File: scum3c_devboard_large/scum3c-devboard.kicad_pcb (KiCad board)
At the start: 2 copper layers, 39.3 x 76.2 mm, 62 parts, among them J1 CONSMA001-SMD-G-T, J2 47346-0001, J3 Conn_02x06_Odd_Even, J4 Conn_01x23, J5 Conn_02x02_Odd_Even, J6 Conn_02x02_Odd_Even, U1 Perfboard, U2 FT231XS-U, U3 74AVC1T45GS,132, U4 74AVC1T45GS,132, U5 LP5907MFX-1.5, U6 S-85S1AB10-I6T1U, U7 S-85S1AB15-I6T1U, U8 scum3, U9AB1 MPU-9250

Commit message: ready for merge
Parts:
- removed C12, C8: LED, Capacitor_SMD:C_0402_1005Metric
- removed C13, C14, C15, C16, C17, C18, C19, C20, C21, C22, C24: NP, Capacitor_SMD:C_0402_1005Metric
- removed NT1: Net-Tie_2, NetTie:NetTie-2_SMD_Pad0.5mm
- removed R12, R13, R14, R5, R6: NP, Resistor_SMD:R_0402_1005Metric
- added D1: LED, LED_SMD:LED_0402_1005Metric, F.Cu at (209.9, 95.6)
- added D2: LED, LED_SMD:LED_0402_1005Metric, F.Cu at (207.0, 87.0)
- added IC1: 74AVC4TD245PW,118, SamacSys_Parts:SOP65P640X110-16N, F.Cu at (223.1, 122.7)
- added IC2: 74AVC4TD245PW,118, SamacSys_Parts:SOP65P640X110-16N, F.Cu at (223.0, 96.5)
- added J7: Conn_01x03, Connector_PinHeader_2.54mm:PinHeader_1x03_P2.54mm_Vertical, F.Cu at (201.5, 112.5)
- added J8: Conn_01x03, Connector_PinHeader_2.54mm:PinHeader_1x03_P2.54mm_Vertical, F.Cu at (205.2, 116.5)
- H1, H2, H3, H4: footprint MountingHole:MountingHole_2.7mm -> MountingHole:MountingHole_2.7mm_M2.5
- J4: value Conn_01x23 -> Conn_01x22; footprint Connector_PinHeader_2.54mm:PinHeader_1x23_P2.54mm_Vertical -> Connector_PinHeader_2.54mm:PinHeader_1x22_P2.54mm_Vertical
- J5: value Conn_02x02_Odd_Even -> Conn_02x04_Odd_Even; footprint Connector_PinHeader_2.54mm:PinHeader_2x02_P2.54mm_Vertical -> Connector_PinHeader_2.54mm:PinHeader_2x04_P2.54mm_Vertical
- J6: value Conn_02x02_Odd_Even -> Conn_01x03; footprint Connector_PinHeader_2.54mm:PinHeader_2x02_P2.54mm_Vertical -> Connector_PinHeader_2.54mm:PinHeader_1x03_P2.54mm_Vertical
- moved J5 51.3 mm to (196.5, 119.9)
- moved J6 51.2 mm to (201.5, 116.2)
- moved C25 48.0 mm to (220.2, 127.0)
- moved L2 48.0 mm to (221.8, 127.5)
- moved U6 48.0 mm to (224.4, 127.0)
- moved C9 48.0 mm to (226.4, 127.1), turned to 270 degrees
- moved U1 37.4 mm to (201.5, 75.4), turned to 90 degrees
- moved C23 24.8 mm to (201.7, 124.5), turned to 90 degrees
- moved U7 20.1 mm to (203.7, 125.3), turned to 180 degrees
- moved L3 15.0 mm to (206.3, 124.7), turned to 180 degrees
- moved C26 14.2 mm to (220.2, 88.2)
- moved C29 14.2 mm to (223.2, 87.9)
- moved U9AB1 14.2 mm to (224.0, 90.7)
- moved C27 14.1 mm to (225.9, 88.0)
- moved U3 12.8 mm to (217.6, 92.5), turned to 0 degrees
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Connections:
- C28 pad 1: +VBAT -> /VBAT_TEENSY
- C3 pad 1: +VBAT -> /VBAT_USB
- J4 pad 1: GND -> +VIN
- J4 pad 10: /3WB_CLK -> /3WB_ENB
- J4 pad 11: /3WB_ENB -> /3WB_DATA
- J4 pad 12: /3WB_DATA -> /GPIO0
- J4 pad 13: /GPIO0 -> GND
- J4 pad 14: GND -> Net-(J4-Pad14)
- J4 pad 16: Net-(J4-Pad16) -> /GPIO3
- J4 pad 17: /GPIO3 -> /Teensy Connections/aPHIb33
- J4 pad 18: /aPHIb -> /Teensy Connections/aPHI33
- J4 pad 19: /aPHI -> /Teensy Connections/aSCANOUT33
- J4 pad 2: +VIN -> /Teensy Connections/aSCSEL33
- J4 pad 20: /aSCANOUT -> /Teensy Connections/aLOAD33
- J4 pad 21: /aLOAD -> /Rx33
- J4 pad 22: /RsRx -> /Tx33
- J4 pad 3: /aSCANIN -> /Teensy Connections/aSCANIN33
- J4 pad 4: /aSCSEL -> /GPIO1
- J4 pad 5: /GPIO1 -> /Teensy Connections/Clock33
- J4 pad 6: /Clock -> /GPIO2
- J4 pad 7: /GPIO2 -> /sReset
- J4 pad 8: /sReset -> /Teensy Connections/hReset33
- J4 pad 9: /hReset -> /3WB_CLK
- J5 pad 1: /1Vin -> /Boot_Source_Sel
- J5 pad 4: +VBAT -> GND
- J6 pad 2: /Boot_Source_Sel -> +VDDIO
- J6 pad 3: +VDDIO -> +VBAT
- L3 pad 1: +VBAT -> /VBAT_TEENSY
- U2 pad 20: /UART/RsRx33 -> /Rx33
- U2 pad 4: /UART/RsTx33 -> /Tx33
- U3 pad 4: /UART/RsRx33 -> /Rx33
- U4 pad 4: /UART/RsTx33 -> /Tx33
- U5 pad 5: Net-(NT1-Pad1) -> /VBAT_USB
- U7 pad 1: +VBAT -> /VBAT_TEENSY
- U8 pad 10: +VDD25 -> Net-(U8-Pad10)
- U8 pad 12: /scumsheet/VDD_AO_DISABLE -> Net-(U8-Pad12)
- U8 pad 70: /scumsheet/AUX_LDO_OUTPUT -> Net-(U8-Pad70)
- U8 pad 71: /scumsheet/VDDD_DISABLE -> Net-(U8-Pad71)
- U8 pad 72: +VDDD -> Net-(U8-Pad72)
- U8 pad 92: +VDDAO -> Net-(U8-Pad92)
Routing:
- net +UART33: track 56.5 -> 107.1 mm
- net /Teensy Connections/aLOAD33: track 0.00 -> 47.7 mm
- net /Rx33: track 0.00 -> 45.2 mm, vias 0 -> 2
- net /Teensy Connections/aSCANOUT33: track 0.00 -> 44.3 mm
- net +VBAT: track 152.1 -> 108.5 mm, vias 6 -> 7
- net /RsRx: track 54.9 -> 12.2 mm, vias 3 -> 2
- net /Tx33: track 0.00 -> 36.0 mm, vias 0 -> 2
- net /RsTx: track 53.2 -> 17.7 mm, vias 3 -> 2
- net /Teensy Connections/Clock33: track 0.00 -> 28.5 mm, vias 0 -> 2
- net /Clock: track 30.7 -> 8.56 mm, vias 1 -> 0
- net /hReset: track 27.7 -> 8.57 mm, vias 1 -> 2
- net +VDDD: track 44.3 -> 25.8 mm, vias 1 -> 0
- net +VDDIO: track 79.4 -> 97.6 mm, vias 3 -> 7
- net /Teensy Connections/hReset33: track 0.00 -> 17.4 mm, vias 0 -> 1
- net +VIN: track 82.0 -> 66.4 mm
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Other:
- board size 39.3 x 76.2 mm -> 39 x 69.1 mm

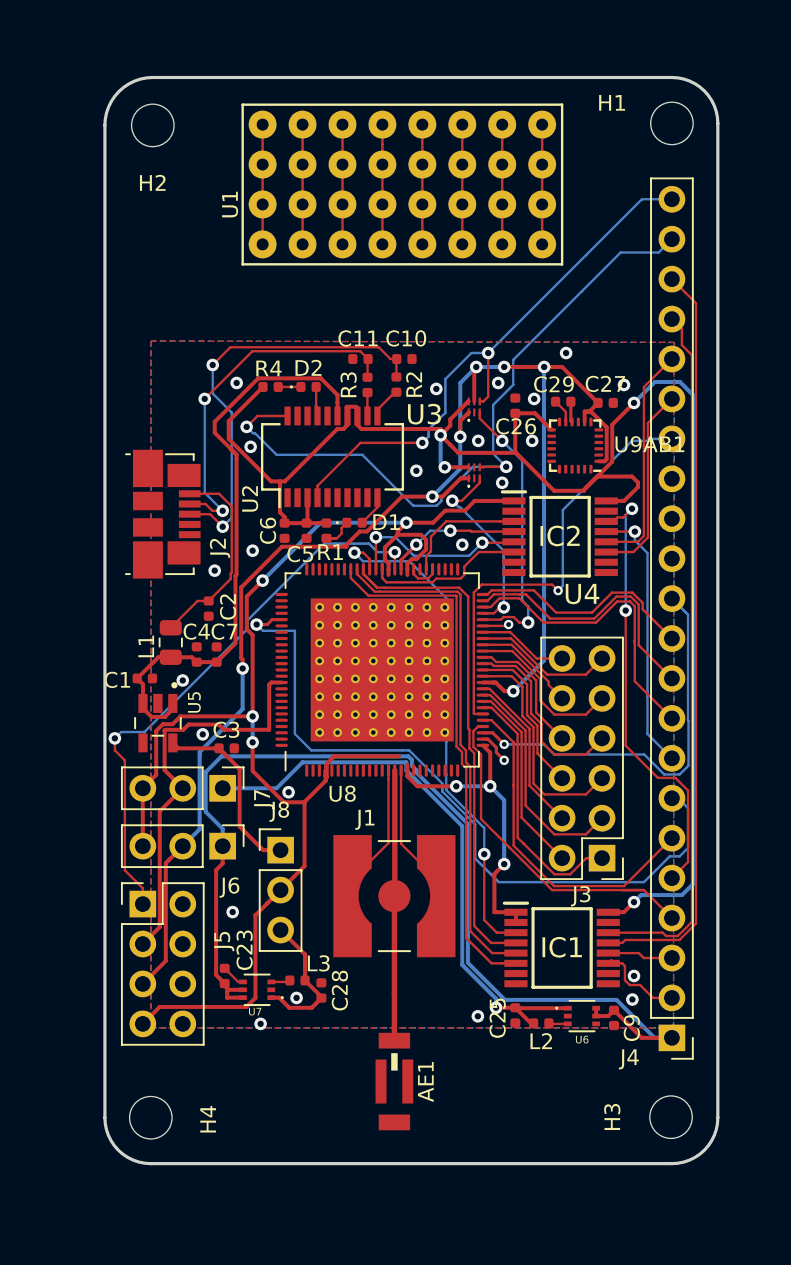
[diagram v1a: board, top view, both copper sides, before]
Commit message: replaced level shifters and other changes
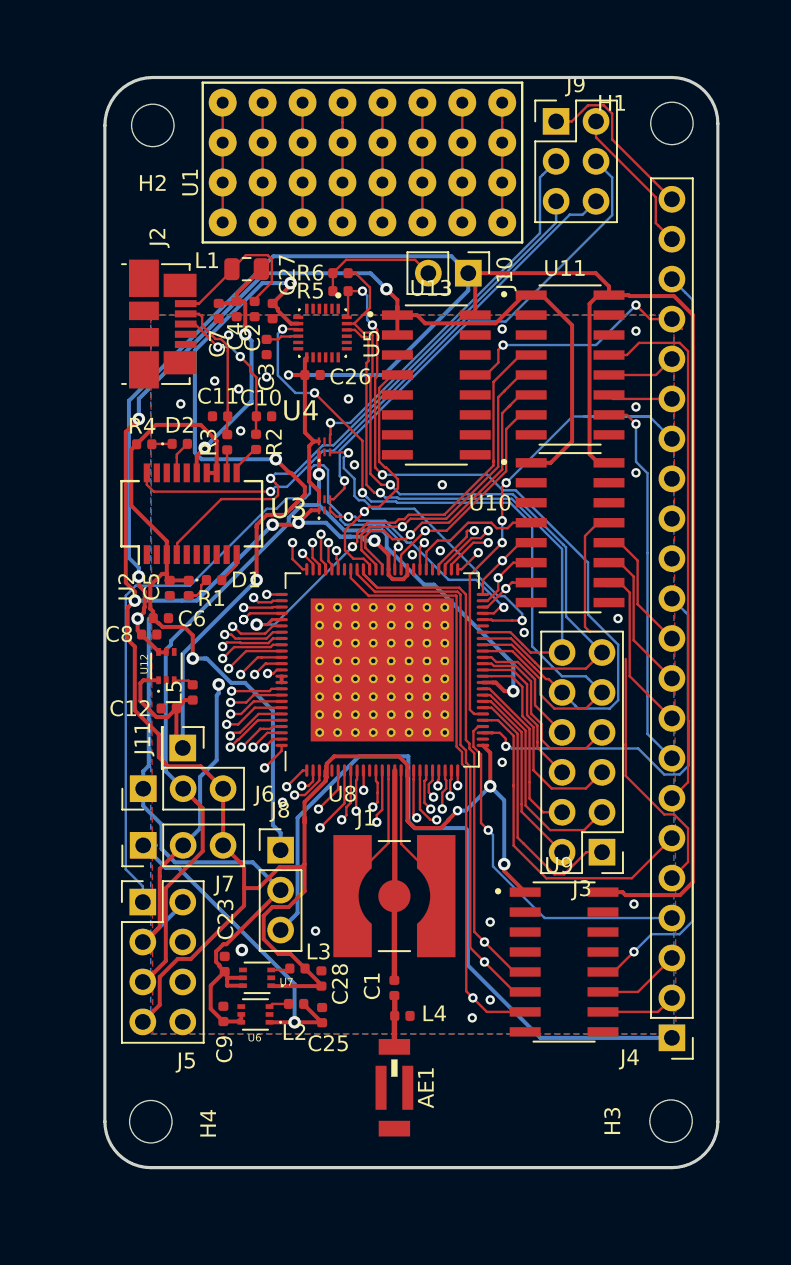
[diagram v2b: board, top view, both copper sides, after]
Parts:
- removed C29: 0.1uF, Capacitor_SMD:C_0402_1005Metric
- removed IC1, IC2: 74AVC4TD245PW,118, SamacSys_Parts:SOP65P640X110-16N
- removed U9AB1: MPU-9250, Sensor_Motion:InvenSense_QFN-24_3x3mm_P0.4mm
- added C12: 10 uF, Capacitor_SMD:C_0402_1005Metric, F.Cu at (198.1, 107.4)
- added C8: 10 uF, Capacitor_SMD:C_0402_1005Metric, F.Cu at (196.9, 102.7)
- added J10: Conn_01x02, Connector_PinHeader_2.54mm:PinHeader_1x02_P2.54mm_Vertical, F.Cu at (217.2, 79.8)
- added J11: Conn_01x01, Connector_PinHeader_2.54mm:PinHeader_1x01_P2.54mm_Vertical, F.Cu at (199.0, 110.0)
- added J9: Conn_02x03_Odd_Even, Connector_PinHeader_2.54mm:PinHeader_2x03_P2.54mm_Vertical, F.Cu at (222.8, 70.1)
- added L4: 3.9 nH, Inductor_SMD:L_0402_1005Metric, F.Cu at (213.0, 127.0)
- added L5: 2.2 uH, Inductor_SMD:L_0402_1005Metric, F.Cu at (199.6, 106.4)
- added R5: 10k, Resistor_SMD:R_0402_1005Metric, F.Cu at (209.0, 80.9)
- added R6: 10k, Resistor_SMD:R_0402_1005Metric, F.Cu at (209.0, 79.8)
- added U10: 74AVCH4T245D,118, downloaded_libs:SOIC127P600X175-16N, F.Cu at (223.6, 96.3)
- added U11: 74AVCH4T245D,118, downloaded_libs:SOIC127P600X175-16N, F.Cu at (223.6, 85.6)
- added U12: S-85S1AB18-I6T1U, downloaded_libs:SOFL50P180X50-6N, F.Cu at (198.0, 104.7)
- added U13: 74AVCH4T245D,118, downloaded_libs:SOIC127P600X175-16N, F.Cu at (215.1, 86.9)
- added U9: 74AVCH4T245D,118, downloaded_libs:SOIC127P600X175-16N, F.Cu at (223.3, 123.6)
- C1: value 10uF -> 1.5 pF
- C3: value 10uF -> 0.1uF
- U5: value LP5907MFX-1.5 -> ICM-20948; footprint downloaded_libs:SOT95P280X145-5N -> downloaded_libs:QFN40P300X300X105-24N
- moved U5 26.9 mm to (207.9, 83.6)
- moved C3 25.7 mm to (204.3, 84.5), turned to 90 degrees
- moved C1 25.3 mm to (212.5, 125.2), turned to 90 degrees
- moved C9 24.8 mm to (201.6, 126.9), turned to 90 degrees
- moved L1 24.2 mm to (203.1, 79.5), turned to 0 degrees
- moved C4 22.1 mm to (202.4, 82.0), turned to 270 degrees
- moved C27 22.0 mm to (204.7, 82.2), turned to 270 degrees
- moved C7 21.8 mm to (201.3, 82.2), turned to 270 degrees
- moved U6 20.8 mm to (203.6, 126.9), turned to 180 degrees
- moved C2 19.3 mm to (203.6, 82.0)
- moved L2 15.6 mm to (206.2, 126.2), turned to 180 degrees
- moved C26 13.0 mm to (207.3, 86.2), turned to 0 degrees
- moved C25 12.3 mm to (207.9, 127.0), turned to 90 degrees
- moved J2 12.1 mm to (197.7, 83.0)
- moved U4 9.86 mm to (208.0, 90.8)
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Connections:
- AE1 pad 1: /RF_IN -> Net-(AE1-Pad1)
- C1 pad 1: GND -> Net-(AE1-Pad1)
- C1 pad 2: +VUSB -> /RF_IN
- C26 pad 1: +UART33 -> +VIN
- C27 pad 1: +VDDIO -> +V18IO
- C28 pad 1: /VBAT_TEENSY -> +VBAT
- C3 pad 1: /VBAT_USB -> GND
- C3 pad 2: GND -> Net-(C3-Pad2)
- J4 pad 1: +VIN -> +TEENSY33
- J4 pad 10: /3WB_ENB -> /Teensy Connections/3WB_ENB33
- J4 pad 11: /3WB_DATA -> /Teensy Connections/3WB_DATA33
- J4 pad 7: /sReset -> /Teensy Connections/sReset33
- J4 pad 9: /3WB_CLK -> /Teensy Connections/3WB_CLK33
- J5 pad 2: Net-(J5-Pad2) -> +VDDD
- J8 pad 1: /VBAT_USB -> +UART33
- J8 pad 2: +VBAT -> +VIN
- J8 pad 3: /VBAT_TEENSY -> +TEENSY33
- L3 pad 1: /VBAT_TEENSY -> +VBAT
- U2 pad 20: /Rx33 -> /UART/RsRx33USB
- U2 pad 4: /Tx33 -> /UART/RsTx33USB
- U3 pad 1: +VDDIO -> +VBAT
- U3 pad 4: /Rx33 -> /UART/RsRx33
- U3 pad 6: +UART33 -> +VIN
- U4 pad 4: /Tx33 -> /UART/RsTx33
- U4 pad 5: +VDDIO -> GND
- U4 pad 6: +UART33 -> +VIN
- U5 pad 1: +VUSB -> Net-(U5-Pad1)
- U5 pad 2: GND -> Net-(U5-Pad1)
- U5 pad 3: +VUSB -> Net-(U5-Pad1)
- U5 pad 4: (no net) -> Net-(U5-Pad1)
- U5 pad 5: /VBAT_USB -> Net-(U5-Pad1)
- U7 pad 1: /VBAT_TEENSY -> +VBAT
- U8 pad 89: Net-(U8-Pad89) -> +VDDD
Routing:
- net +VIN: track 66.4 -> 182.6 mm, vias 0 -> 3
- net +VBAT: track 108.5 -> 173.4 mm, vias 7 -> 9
- net +UART33: track 107.1 -> 43.3 mm, vias 4 -> 1
- net +V18IO: track 0.00 -> 57.3 mm, vias 0 -> 3
- net +TEENSY33: track 0.00 -> 47.9 mm
- net /GPIO13: track 6.58 -> 50.8 mm, vias 0 -> 3
- net /GPIO12: track 10.5 -> 50.1 mm, vias 0 -> 3
- net /UART/RsRx33USB: track 0.00 -> 37.2 mm, vias 0 -> 1
- net /GPIO14: track 8.96 -> 46.1 mm, vias 0 -> 1
- net /UART/RsTx33USB: track 0.00 -> 36.0 mm, vias 0 -> 1
- net /Rx33: track 45.2 -> 9.49 mm, vias 2 -> 0
- net +VDDIO: track 97.6 -> 62.0 mm, vias 7 -> 2
- net /Teensy Connections/sReset33: track 0.00 -> 34.8 mm
- net /GPIO15: track 5.73 -> 37.2 mm, vias 0 -> 1
- net /UART/RsRx33: track 0.00 -> 31.1 mm, vias 0 -> 1
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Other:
- board size 39 x 69.1 mm -> 39 x 69.3 mm

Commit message: clean up labels
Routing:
- net /1Vin: track 21.7 -> 20.9 mm
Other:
- board text added: "1.8V"
- board text added: "1V"
- board text added: "Development Region"
- board text added: "GPIO"
- board text added: "I2C Pullup"
- board text added: "IMU"
- board text added: "TEENSY 3.3"
- board text added: "Teensy Pin 23"
- board text added: "Teensy Pin 33"
- board text added: "Teensy Rx/Tx"
- board text added: "UART 3.3"
- board text added: "USB"
- board text added: "USB Rx/Tx"
- board text added: "VBAT"
- board text added: "VDDD"
- board text added: "VDDD Source"
- board text added: "VDDIO"
- board text added: "VDDIO Source"
- board text added: "VIN"
- board text added: "VIN Source"
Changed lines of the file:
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@@
   (general
     (thickness 0.7874)
-    (drawings 8)
-    (tracks 1386)
+    (drawings 30)
+    (tracks 1385)
     (zones 0)
     (modules 59)
@@
     (32 B.Adhes user)
     (33 F.Adhes user)
-    (34 B.Paste user)
-    (35 F.Paste user)
     (36 B.SilkS user)
     (37 F.SilkS user)
@@
     (47 F.CrtYd user)
     (48 B.Fab user)
-    (49 F.Fab user hide)
+    (49 F.Fab user)
   )
   (setup
@@
   (module downloaded_libs:QFN40P300X300X105-24N (layer F.Cu)
     (at 207.899 83.566 270)
-    (fp_text reference U5 (at 0.675 -3.135 270) (layer F.SilkS)
+    (fp_text reference U5 (at 7.6708 -2.9972 270) (layer F.SilkS)
       (effects (font (size 1 1) (thickness 0.015)))
     )
@@
     (descr "Through hole straight pin header, 2x03, 2.54mm pitch, double rows")
     (tags "Through hole pin header THT 2x03 2.54mm double row")
-    (fp_text reference J9 (at 1.27 -2.33) (layer F.SilkS)
+    (fp_text reference J9 (at 4.8006 5.1054) (layer F.SilkS)
       (effects (font (size 1 1) (thickness 0.15)))
     )
@@
     (tags "mounting hole 2.7mm no annular m2.5")
     (attr virtual)
-    (fp_text reference H2 (at 0 -3.7 180) (layer F.SilkS)
+    (fp_text reference H2 (at -0.0508 2.159 180) (layer F.SilkS)
       (effects (font (size 1 1) (thickness 0.15)))
     )
@@
     (tags "mounting hole 2.7mm no annular m2.5")
     (attr virtual)
-    (fp_text reference H1 (at 3.81 1.27 180) (layer F.SilkS)
+    (fp_text reference H1 (at -0.0508 2.0828 180) (layer F.SilkS)
       (effects (font (size 1 1) (thickness 0.15)))
     )
@@
     (tags inductor)
     (attr smd)
-    (fp_text reference L3 (at -1.34112 1.05049 180) (layer F.SilkS)
+    (fp_text reference L3 (at -1.06172 0.92349 180) (layer F.SilkS)
       (effects (font (size 1 1) (thickness 0.15)))
     )
@@
   (module SCUM:Perfboard (layer F.Cu)
     (at 199.009 73.9902 90)
-    (fp_text reference U1 (at 0 0.5 90) (layer F.SilkS)
+    (fp_text reference U1 (at -2.8702 0.635 90) (layer F.SilkS)
       (effects (font (size 1 1) (thickness 0.15)))
     )
@@
     )
   )
+  (gr_text "TEENSY 3.3" (at 207.0354 121.031 270) (layer F.SilkS)
+    (effects (font (size 0.3062 0.3062) (thickness 0.07655)))
+  )
+  (gr_text "UART 3.3" (at 207.0608 116.4844 270) (layer F.SilkS)
+    (effects (font (size 0.3062 0.3062) (thickness 0.07655)))
+  )
+  (gr_text 1.8V (at 199.009 108.2802) (layer F.SilkS)
+    (effects (font (size 0.3062 0.3062) (thickness 0.07655)))
+  )
+  (gr_text VIN (at 196.4944 110.744) (layer F.SilkS)
+    (effects (font (size 0.3062 0.3062) (thickness 0.07655)))
+  )
+  (gr_text VBAT (at 201.549 110.6678) (layer F.SilkS)
+    (effects (font (size 0.3062 0.3062) (thickness 0.07655)))
+  )
+  (gr_text VBAT (at 201.5744 114.3508) (layer F.SilkS)
+    (effects (font (size 0.3062 0.3062) (thickness 0.07655)))
+  )
+  (gr_text 1V (at 196.5198 114.3508) (layer F.SilkS)
+    (effects (font (size 0.3062 0.3062) (thickness 0.07655)))
+  )
+  (gr_text "USB Rx/Tx" (at 224.0534 77.4192) (layer F.SilkS)
+    (effects (font (size 0.484 0.484) (thickness 0.0968)))
+  )
+  (gr_text USB (at 196.088 88.0618) (layer F.SilkS)
+    (effects (font (size 0.484 0.484) (thickness 0.0968)))
+  )
+  (gr_text IMU (at 210.4136 83.8708 270) (layer F.SilkS)
+    (effects (font (size 0.484 0.484) (thickness 0.0968)))
+  )
+  (gr_text GPIO (at 221.234 110.1852 90) (layer F.SilkS)
+    (effects (font (size 0.484 0.484) (thickness 0.0968)))
+  )
+  (gr_text "I2C Pullup" (at 210.7438 78.6384) (layer F.SilkS)
+    (effects (font (size 0.484 0.484) (thickness 0.0968)))
+  )
+  (gr_text "VIN Source" (at 207.518 119.0498 270) (layer F.SilkS)
+    (effects (font (size 0.3062 0.3062) (thickness 0.07655)))
+  )
+  (gr_text "VDDD Source" (at 194.5894 116.1796 270) (layer F.SilkS)
+    (effects (font (size 0.3062 0.3062) (thickness 0.07655)))
+  )
+  (gr_text "Teensy Rx/Tx" (at 224.028 67.9196) (layer F.SilkS)
+    (effects (font (size 0.484 0.484) (thickness 0.0968)))
+  )
+  (gr_text "Teensy Pin 33" (at 232.41 75.0316 90) (layer F.SilkS)
+    (effects (font (size 0.484 0.484) (thickness 0.0968)))
+  )
+  (gr_text "Teensy Pin 23" (at 232.41 125.9078 90) (layer F.SilkS)
+    (effects (font (size 0.484 0.484) (thickness 0.0968)))
+  )
+  (gr_text "Development\nRegion" (at 197.8914 74.168) (layer F.SilkS)
+    (effects (font (size 0.484 0.484) (thickness 0.0968)))
+  )
+  (gr_text "VDDIO Source" (at 194.5894 112.5474 270) (layer F.SilkS)
+    (effects (font (size 0.3062 0.3062) (thickness 0.07655)))
+  )
+  (gr_text VDDD (at 194.564 122.047 270) (layer F.SilkS)
+    (effects (font (size 0.5094 0.5094) (thickness 0.1222)))
+  )
+  (gr_text VDDIO (at 194.564 124.714 270) (layer F.SilkS)
+    (effects (font (size 0.5094 0.5094) (thickness 0.1222)))
+  )
+  (gr_text VBAT (at 194.564 127.4826 270) (layer F.SilkS)
+    (effects (font (size 0.5094 0.5094) (thickness 0.1222)))
+  )
   (gr_line (start 197.104 67.31) (end 230.124 67.31) (layer Edge.Cuts) (width 0.2))
   (gr_line (start 194.056 133.731) (end 194.056 70.358) (layer Edge.Cuts) (width 0.2))
@@
   (segment (start 209.371 118.7276) (end 212.09737 116.00123) (width 0.1524) (layer F.Cu) (net 2))
   (segment (start 212.09737 116.00123) (end 212.09737 111.94691) (width 0.1524) (layer F.Cu) (net 2))
-  (via (at 207.4545 121.6025) (size 0.6) (drill 0.3) (layers F.Cu B.Cu) (net 2))
+  (via (at 207.6704 121.6025) (size 0.6) (drill 0.3) (layers F.Cu B.Cu) (net 2))
   (via (at 198.882 88.0745) (size 0.6) (drill 0.3) (layers F.Cu B.Cu) (net 2))
   (via (at 202.7682 122.809) (size 0.8) (drill 0.4) (layers F.Cu B.Cu) (net 2))
@@
   (segment (start 206.705554 126.270164) (end 207.871554 127.436164) (width 0.254) (layer F.Cu) (net 102))
   (segment (start 206.705554 126.238) (end 206.705554 126.270164) (width 0.254) (layer F.Cu) (net 102))
-  (segment (start 197.3072 116.1542) (end 196.4944 116.1542) (width 0.254) (layer B.Cu) (net 102))
   (segment (start 206.121 127.407163) (end 206.121 124.968) (width 0.254) (layer B.Cu) (net 102))
   (segment (start 198.738209 117.585209) (end 206.121 124.968) (width 0.254) (layer B.Cu) (net 102))
